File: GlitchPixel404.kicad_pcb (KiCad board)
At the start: 2 copper layers, 50 x 34 mm, 59 parts, among them J1 USB_C_Receptacle_USB2.0_16P, J2 VOLTLINK, J5 Barrel_Jack_Switch, J7 Output, Q1 AONR21357-ES, Q2 MMBT3904, SW1 Reset, SW3 SW_SP3T, U1 ESP32-PICO-MINI-02U-N8R2, U2 TPS54202DDC, U3 CH224K, U4 CH340N, U5 IRM-H6xxT, U6 74LVC2G34, U7 HE2021A50HMR, U8 74LVC2G34

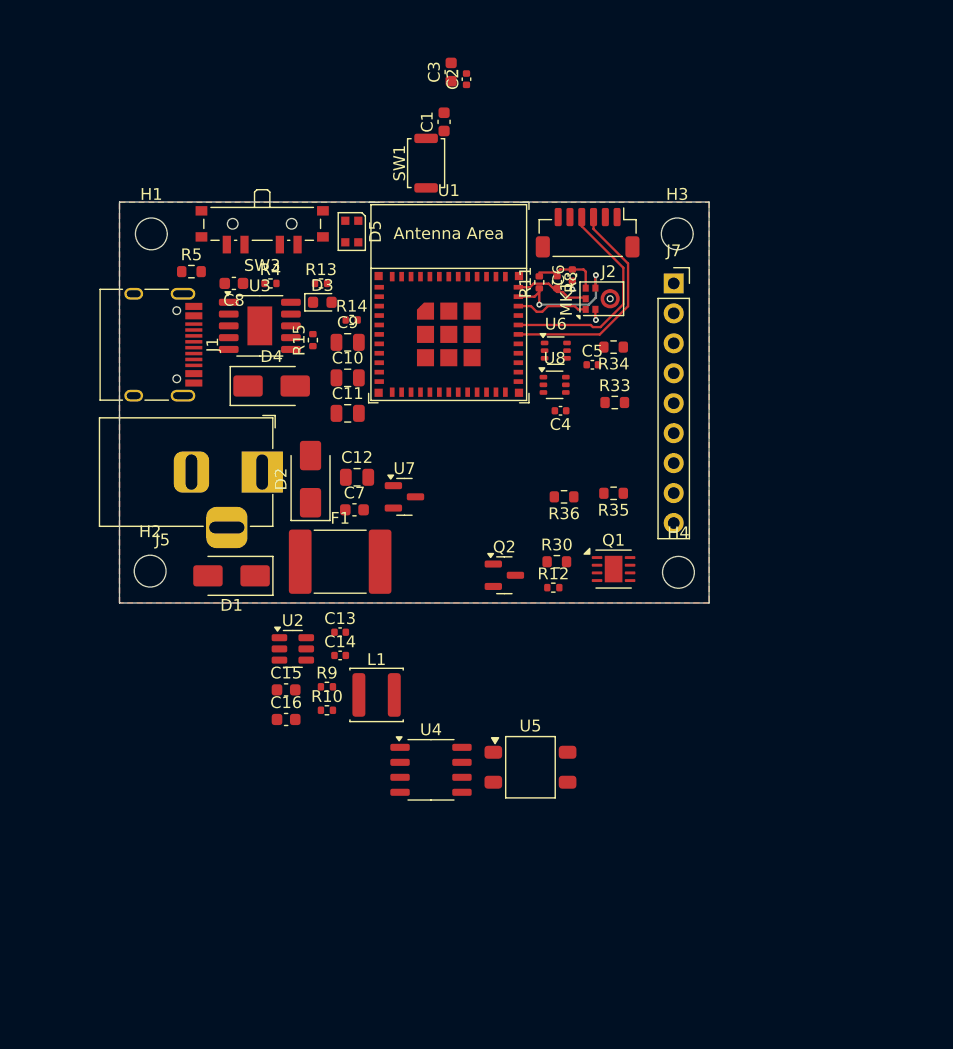
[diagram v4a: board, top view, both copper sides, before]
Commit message: Added fet protection and started layout
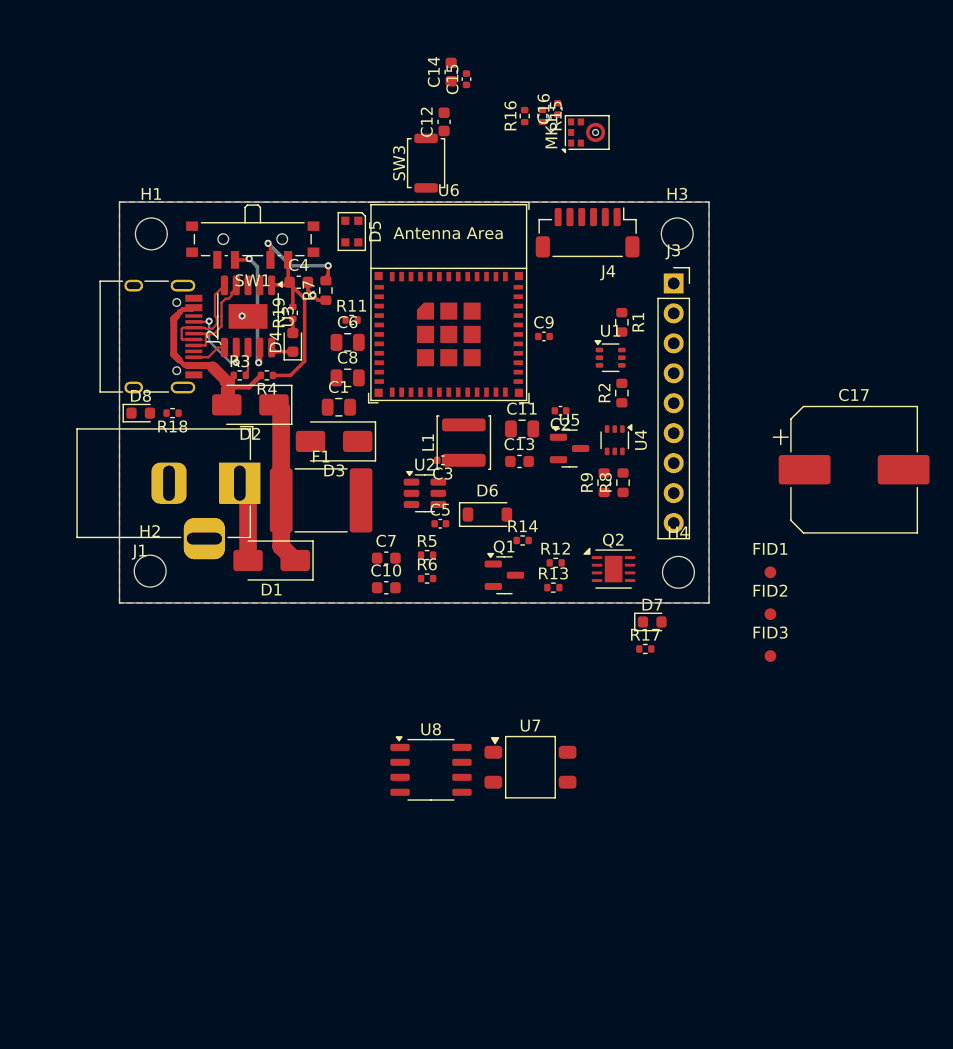
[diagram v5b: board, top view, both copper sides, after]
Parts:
- removed the R13 at (117.1, 72.9)
- removed R30: 2k2, Resistor_SMD:R_0603_1608Metric
- added C17: 680uF, Capacitor_SMD:CP_Elec_10x12.5, F.Cu at (162.3, 88.7)
- added D6: 10V, Diode_SMD:D_SOD-123, F.Cu at (131.2, 92.5)
- added D7: Green, LED_SMD:LED_0603_1608Metric, F.Cu at (145.2, 101.6)
- added D8: Green, LED_SMD:LED_0603_1608Metric, F.Cu at (101.8, 83.9)
- added FID1: Fiducial, Fiducial:Fiducial_1mm_Mask2mm, F.Cu at (155.2, 97.4)
- added FID2: Fiducial, Fiducial:Fiducial_1mm_Mask2mm, F.Cu at (155.2, 101.0)
- added FID3: Fiducial, Fiducial:Fiducial_1mm_Mask2mm, F.Cu at (155.2, 104.5)
- added R12: 10k, Resistor_SMD:R_0402_1005Metric, F.Cu at (137.0, 96.6)
- added R14: 1k, Resistor_SMD:R_0402_1005Metric, F.Cu at (134.2, 94.7)
- added R17: 10k, Resistor_SMD:R_0402_1005Metric, F.Cu at (144.6, 103.9)
- added R18: 10k, Resistor_SMD:R_0402_1005Metric, F.Cu at (104.5, 83.9)
- added R19: 1k, Resistor_SMD:R_0402_1005Metric, F.Cu at (114.7, 75.4)
- D4: renamed from D3; value LED_Small -> Yellow
- moved L1 22.6 mm to (129.2, 86.4), turned to 90 degrees
- moved U2 17.3 mm to (125.9, 90.7)
- moved C3 17.0 mm to (127.4, 87.9), turned to 180 degrees
- moved C11 14.6 mm to (134.1, 85.2)
- moved C13 14.6 mm to (133.9, 88.0)
- moved U5 14.6 mm to (138.2, 86.9)
- moved C16 14.2 mm to (137.2, 58.1)
- moved MK1 14.2 mm to (139.7, 60.1)
- moved R16 14.2 mm to (134.4, 58.7)
- moved R15 14.2 mm to (135.9, 58.7)
- moved C10 14.0 mm to (122.6, 98.7)
- moved C5 14.0 mm to (127.2, 93.3)
- moved C7 14.0 mm to (122.6, 96.2)
- moved R5 14.0 mm to (126.1, 95.9)
- moved R6 14.0 mm to (126.1, 97.9)
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- renumbered C11 to C1, C16 to C10, C12 to C11, C1 to C12, C7 to C13, C3 to C14, C2 to C15, C6 to C16, C4 to C2, C13 to C3, C8 to C4, C14 to C5, C9 to C6, C15 to C7, C10 to C8, C5 to C9, D4 to D3, J5 to J1, J1 to J2, J7 to J3, J2 to J4, Q2 to Q1, Q1 to Q2, R34 to R1, R14 to R11, R12 to R13, R8 to R15, R11 to R16, R33 to R2, R15 to R3, R9 to R5, R10 to R6, R5 to R7, R35 to R8, R36 to R9, SW3 to SW1, SW1 to SW3, U6 to U1, U8 to U4, U7 to U5, U1 to U6, U5 to U7, U4 to U8
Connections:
- net Net-(D1-K) renamed /Vcmb
- net Net-(J1-CC1) renamed /CC1
- net Net-(J1-CC2) renamed /CC2
- net Net-(U2-BOOT) renamed /bst
- net Net-(U2-FB) renamed /fb
- net Net-(U2-SW) renamed /sw
- net Net-(U3-CFG1) renamed /CFG1
- net Net-(U3-DM) renamed /D-
- net Net-(U3-DP) renamed /D+
- net Net-(U3-VBUS) renamed /chVbus
- net PG renamed /PG
- D4 pad 2: Net-(D3-A) -> /lvddpwr
- Q1 pad 1: Net-(Q2-B) -> /Vb
- Q1 pad 3: Net-(Q2-C) -> /Vc
- Q2 pad G: Net-(Q2-C) -> /Vg
- R13 pad 1: Net-(Q2-C) -> /Vg
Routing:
- net VBUS: track 0.00 -> 19.3 mm
- net /RXD: track 19.1 -> 0.00 mm
- net /TXD: track 18.6 -> 0.00 mm
- net VDD: track 0.00 -> 16.3 mm
- net /Vcmb: track 0.00 -> 14.1 mm
- net /CFG1: track 0.00 -> 11.7 mm, vias 0 -> 2
- net SCL: track 11.1 -> 0.00 mm, vias 2 -> 0
- net /D-: track 0.00 -> 8.82 mm
- net /D+: track 0.00 -> 8.73 mm
- net Net-(R7-Pad2): track 0.00 -> 8.73 mm, vias 0 -> 2
- net /CC1: track 0.00 -> 7.33 mm, vias 0 -> 2
- net /VDC: track 0.00 -> 6.85 mm
- net SDA: track 6.36 -> 0.00 mm
- net MIC_WS: track 6.33 -> 0.00 mm
- net +3.3V: track 5.57 -> 0.06 mm
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
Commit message: remove CH340 and start layout
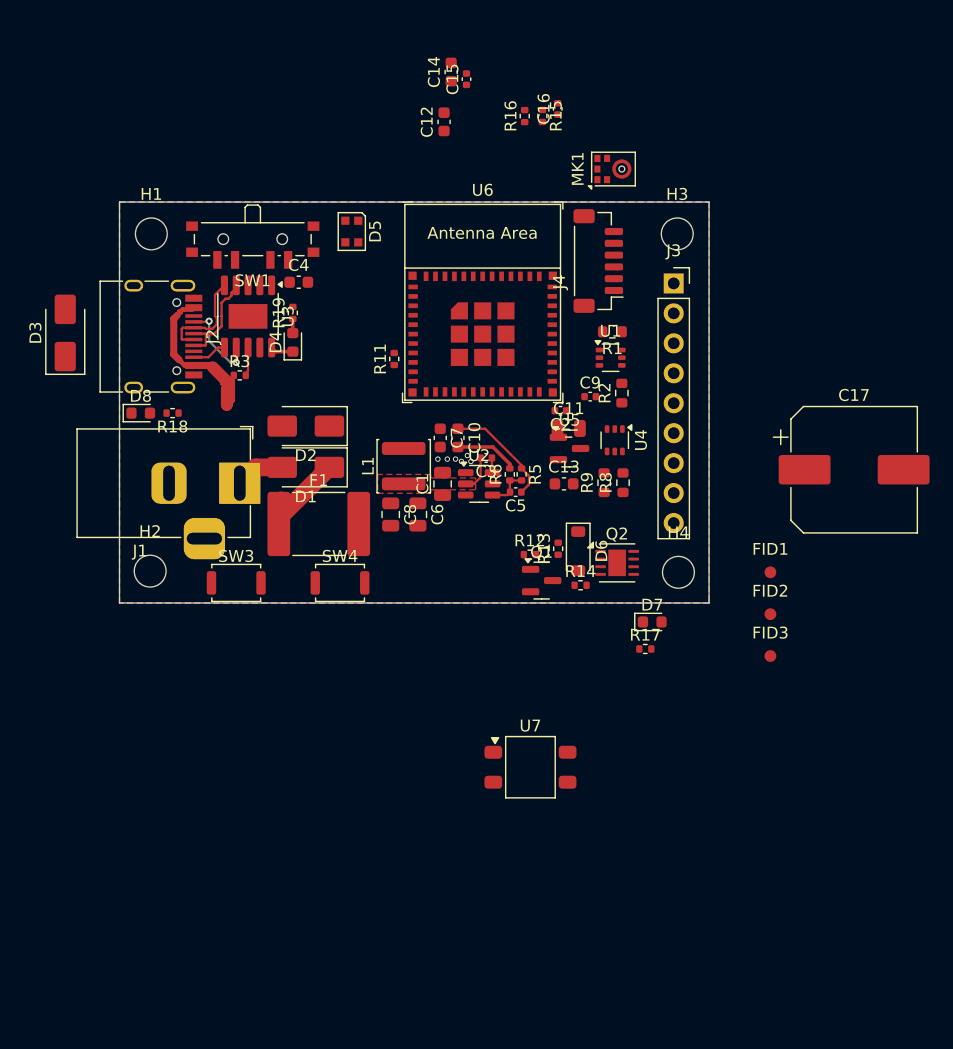
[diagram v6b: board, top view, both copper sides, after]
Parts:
- removed R4: 1k, Resistor_SMD:R_0402_1005Metric
- removed R7: 24k, Resistor_SMD:R_0603_1608Metric
- removed U8: CH340N, Package_SO:SOP-8_3.9x4.9mm_P1.27mm
- added SW4: Boot, Button_Switch_SMD:SW_Push_SPST_NO_Alps_SKRK, F.Cu at (118.7, 98.3)
- moved SW3 39.1 mm to (109.9, 98.3), turned to 0 degrees
- moved D3 24.6 mm to (95.4, 77.1), turned to 90 degrees
- moved C6 15.8 mm to (125.3, 92.5), turned to -90 degrees
- moved C10 14.1 mm to (128.7, 86.0), turned to -90 degrees
- moved C8 12.2 mm to (123.0, 92.5), turned to -90 degrees
- moved R6 11.3 mm to (133.1, 89.1), turned to 90 degrees
- moved C7 11.2 mm to (127.2, 86.0), turned to -90 degrees
- moved C1 10.9 mm to (127.4, 89.9), turned to 90 degrees
- moved R5 10.5 mm to (134.1, 89.1), turned to -90 degrees
- moved D1 8.42 mm to (115.8, 88.5)
- moved D6 8.30 mm to (138.9, 95.6), turned to -90 degrees
- moved C5 6.93 mm to (133.6, 90.6), turned to 180 degrees
- moved C9 6.43 mm to (139.9, 82.5)
- moved R14 6.21 mm to (139.1, 98.5)
- moved L1 5.48 mm to (124.1, 88.4)
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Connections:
- C4 pad 1: VDD -> +3.3V
- R19 pad 2: VDD -> +3.3V
- SW1 pad 1: VDD -> /CFG1
- SW1 pad 2: Net-(R7-Pad2) -> /CFG3
- SW1 pad 3: /CFG1 -> +3.3V
- SW1 pad 4: unconnected-(SW1-Pad4) -> /CFG2
- U3 pad 1: VDD -> +3.3V
- U3 pad 2: unconnected-(U3-CFG2-Pad2) -> /CFG2
- U3 pad 3: unconnected-(U3-CFG3-Pad3) -> /CFG3
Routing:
- net VDD: track 16.3 -> 0.00 mm
- net /CFG1: track 11.7 -> 0.00 mm, vias 2 -> 0
- net +3.3V: track 0.06 -> 9.54 mm
- net Net-(R7-Pad2): track 8.73 -> 0.00 mm, vias 2 -> 0
- net /Vcmb: track 14.1 -> 8.67 mm
- net /fb: track 0.00 -> 3.58 mm
- net VBUS: track 19.3 -> 16.1 mm
- net /sw: track 0.00 -> 3.13 mm
- net GND: track 2.55 -> 5.37 mm, vias 2 -> 6
- net /VDC: track 6.85 -> 4.16 mm
- net /bst: track 0.00 -> 1.27 mm
- added copper zone on F.Cu, net /sw

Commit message: Layout 80% complete, some circuit changes
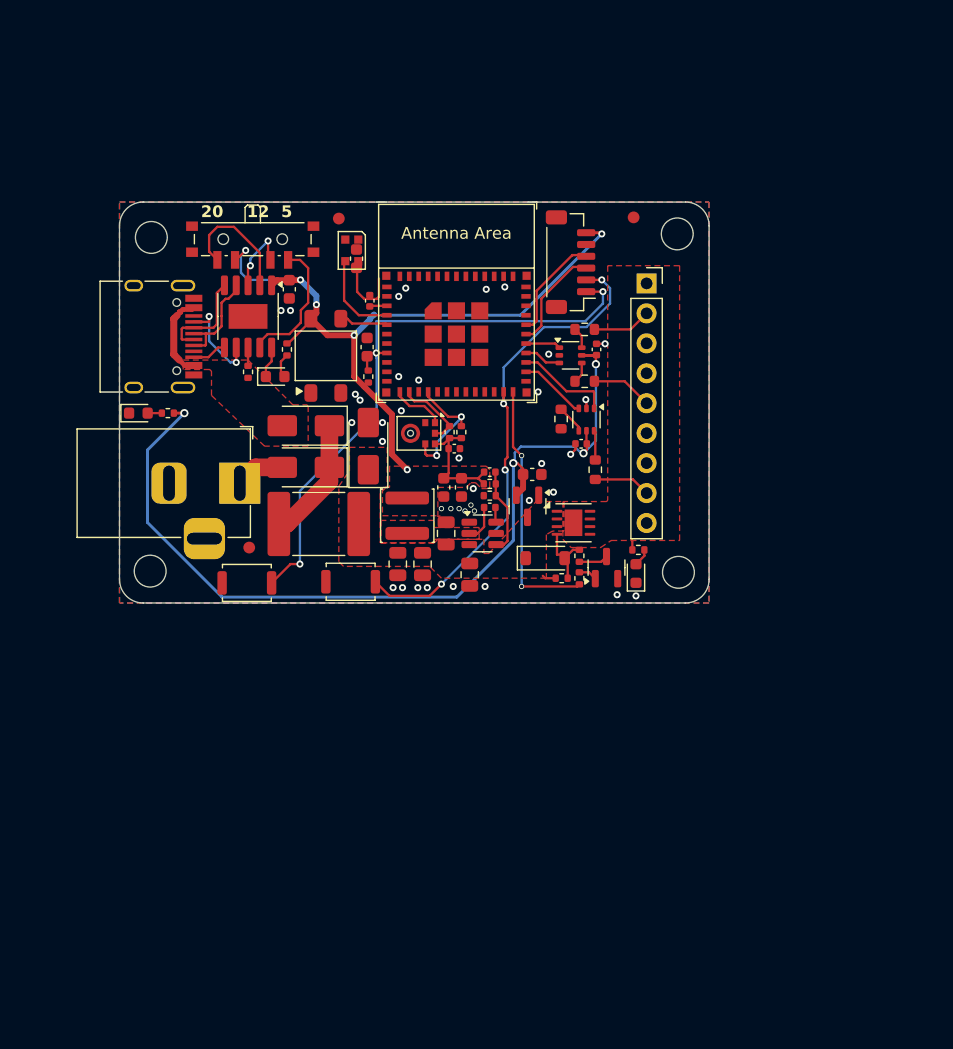
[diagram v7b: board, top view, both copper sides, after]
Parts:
- removed C17: 680uF, Capacitor_SMD:CP_Elec_10x12.5
- moved FID1 47.3 mm to (118.6, 67.4)
- moved FID2 44.6 mm to (111.0, 95.3)
- moved FID3 39.0 mm to (143.6, 67.3)
- moved U7 39.0 mm to (117.5, 79.0), turned to 90 degrees
- moved C16 30.1 mm to (128.4, 86.9), turned to 180 degrees
- moved R15 27.9 mm to (128.0, 85.5), turned to 90 degrees
- moved MK1 27.8 mm to (125.4, 85.6), turned to -90 degrees
- moved D3 27.4 mm to (121.1, 86.7)
- moved R16 27.3 mm to (129.0, 85.5)
- moved C15 20.5 mm to (121.2, 74.4)
- moved C12 20.2 mm to (121.0, 78.3)
- moved C14 17.7 mm to (120.1, 70.8)
- moved C11 15.0 mm to (129.7, 97.6), turned to -90 degrees
- moved R17 8.42 mm to (144.0, 95.5)
- moved R9 6.52 mm to (137.4, 84.4)
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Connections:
- net Net-(D5-DIN) renamed /NEO_OB
- J4 pad 6: /+3V3 -> +3.3V
- U6 pad 12: unconnected-(U6-32K_XP/GPIO32/ADC1_CH4-Pad12) -> MIC_WS
- U6 pad 13: unconnected-(U6-32K_XN/GPIO33/ADC1_CH5-Pad13) -> SDA
- U6 pad 15: unconnected-(U6-GPIO25/ADC2_CH8/DAC_1-Pad15) -> SCL
- U6 pad 24: unconnected-(U6-GPIO4/ADC2_CH0-Pad24) -> SLPwr
- U6 pad 33: MIC_WS -> unconnected-(U6-GPIO19-Pad33)
- U6 pad 34: SCL -> unconnected-(U6-GPIO22-Pad34)
- U6 pad 35: SDA -> unconnected-(U6-GPIO21-Pad35)
- U6 pad 5: unconnected-(U6-SENSOR_CAPP/GPIO37/ADC1_CH1-Pad5) -> IR_Rec
- U7 pad 1: Net-(U7-GND-Pad1) -> GND
- U7 pad 2: Net-(U7-GND-Pad1) -> GND
- U7 pad 3: unconnected-(U7-OUT-Pad3) -> IR_Rec
- U7 pad 4: unconnected-(U7-Vcc-Pad4) -> +3.3V
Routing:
- net +5V: track 0.00 -> 77.7 mm, vias 0 -> 4
- net +3.3V: track 9.54 -> 79.8 mm, vias 0 -> 6
- net /EN: track 0.00 -> 52.1 mm, vias 0 -> 3
- net /IO0: track 0.00 -> 43.5 mm, vias 0 -> 4
- net SLPwr: track 0.00 -> 21.8 mm, vias 0 -> 2
- net /CFG1: track 0.00 -> 11.0 mm
- net SCL: track 0.00 -> 10.8 mm, vias 0 -> 2
- net /CFG2: track 0.00 -> 10.7 mm
- net /TXD: track 0.00 -> 9.11 mm
- net VBUS: track 16.1 -> 7.05 mm
- net /RXD: track 0.00 -> 8.87 mm
- net S3: track 0.00 -> 8.21 mm
- net /NEO_OB: track 0.00 -> 7.52 mm
- net SDA: track 0.00 -> 6.39 mm
- net /CFG3: track 0.00 -> 5.87 mm, vias 0 -> 2
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- added copper zone on F.Cu, net +3.3V
- added copper zone on F.Cu, net LED_PWR
- added copper zone on F.Cu, net VBUS
- added copper zone on F.Cu, net VCC
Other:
- outline, holes or cut-outs redrawn
- board text added: "12"
- board text added: "20"
- board text added: "5"

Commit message: Minor corrections, silk started
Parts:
- removed C9: 100nF, Capacitor_SMD:C_0402_1005Metric
- added D9: Yellow, LED_SMD:LED_0603_1608Metric, F.Cu at (128.5, 87.6)
- added G***: Shroom2mm, Inventel:Shroom_FSilk_2mm, F.Cu at (135.0, 85.7)
- added G***: Shroom3mm, Inventel:Shroom_FSilk_3mm, B.Cu at (128.8, 79.1)
- added J5: Conn_01x03, Connector_PinHeader_2.54mm:PinHeader_1x03_P2.54mm_Vertical, F.Cu at (139.3, 90.3)
- added R20: 10k, Resistor_SMD:R_0402_1005Metric, F.Cu at (126.4, 87.7)
- added kibuzzard-67E14B7B: G***, kibuzzard-67E14B7B, F.Cu at (119.3, 70.9)
- moved FID3 31.4 mm to (143.7, 98.7)
- moved D7 28.2 mm to (143.0, 69.3), turned to 0 degrees
- moved R17 25.0 mm to (142.4, 70.6)
- moved FID2 11.9 mm to (110.8, 83.4)
- moved R8 6.13 mm to (139.7, 82.6), turned to 180 degrees
- moved C2 5.43 mm to (133.9, 87.9), turned to 0 degrees
- moved U4 4.56 mm to (137.5, 80.4), turned to 0 degrees
- moved D5 4.14 mm to (117.2, 73.4), turned to 0 degrees
- moved R18 2.80 mm to (106.9, 84.0), turned to 90 degrees
- moved C14 2.66 mm to (121.0, 73.3)
- moved U1 1.74 mm to (137.9, 77.3)
- moved C15 1.62 mm to (119.7, 73.8)
- moved R16 1.41 mm to (129.0, 84.1)
- moved R15 1.41 mm to (128.0, 84.1)
- moved C16 1.31 mm to (128.5, 85.6)
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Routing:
- net LED_PWR: track 0.94 -> 14.5 mm, vias 0 -> 6
- net GND: track 2.59 -> 14.5 mm, vias 38 -> 46
- net L3: track 4.83 -> 11.9 mm
- net S3: track 8.21 -> 1.93 mm
- net +3.3V: track 79.8 -> 85.0 mm
- net +5V: track 77.7 -> 72.6 mm
- net L4: track 0.00 -> 4.65 mm
- net Net-(D8-A): track 1.20 -> 4.69 mm
- net S4: track 5.76 -> 2.34 mm
- net /NEO_OB: track 7.52 -> 5.24 mm
- net /EN: track 52.1 -> 50.0 mm
- net Net-(U4-1Y): track 2.52 -> 4.32 mm
- net Net-(D9-A): track 0.00 -> 1.48 mm
- net /IO0: track 43.5 -> 42.9 mm
- net MIC_WS: track 4.57 -> 4.04 mm
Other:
- board text added: "+"
- board text added: "-"
- board text added: "3v3"
- board text added: "ESP32-PICO02"
- board text added: "Glitch Pixel 404"
- board text added: "IO0"
- board text added: "IR"
- board text added: "JLCJLCJLC"
- board text added: "L1"
- board text added: "L2"
- board text added: "L3"
- board text added: "L4"
- board text added: "LED Pwr"
- board text added: "Mic"
- board text added: "PG"
- board text added: "PWR"
- board text added: "RA1"
- board text added: "RST"
- board text added: "voltlink"
